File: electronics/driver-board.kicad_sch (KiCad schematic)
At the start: 61 parts, among them J1 Conn_01x18_Female, J3 Motor_Conn_01x04, J4 Screw_Terminals, J5 Conn_01x06_Female, SW1 RST_SW_Push, U1 ESP32-WROOM-E, U2 BA033CC0FP-E2, U4 AS5601-ASOT, U5 TMC2209-LA

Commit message: work on module prototype
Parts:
- removed C25: 10µF, Capacitor_SMD:C_0402_1005Metric, symbol Device:C_Small
- removed C30: 1µF, Capacitor_SMD:C_0402_1005Metric, symbol Device:C_Small
- removed C31, C32, C33: 100nF, Capacitor_SMD:C_0402_1005Metric, symbol Device:C_Small
- removed SW1: RST_SW_Push, Button_Switch_SMD:SW_SPST_B3U-1000P, symbol Switch:SW_Push
- removed TP10, TP11, TP12, TP13, TP14, TP15, TP6, TP7, TP8, TP9: TestPoint, TestPoint:TestPoint_Pad_D1.0mm, symbol Connector:TestPoint
- added J2: Conn_01x02_Socket, Connector_PinSocket_2.54mm:PinSocket_1x02_P2.54mm_Vertical, symbol Connector:Conn_01x02_Socket
- added J7, J8: Conn_01x08_Socket, Connector_PinSocket_2.54mm:PinSocket_1x08_P2.54mm_Vertical, symbol Connector:Conn_01x08_Socket
- added JP2: SolderJumper_3_Bridged12, Jumper:SolderJumper-3_P1.3mm_Bridged12_Pad1.0x1.5mm, symbol Jumper:SolderJumper_3_Bridged12
- added R2: 1K, Resistor_SMD:R_0805_2012Metric_Pad1.20x1.40mm_HandSolder, symbol Device:R_Small
- C10, C11, C12, C13, C14, C15, C16, C8, C9, TP3, TP4, U5: now not fitted; now left out of the parts list
- H2: now not fitted
- R1, R20, R21, R4: footprint Resistor_SMD:R_0402_1005Metric -> Resistor_SMD:R_0805_2012Metric_Pad1.20x1.40mm_HandSolder
- R11: value 1K -> 1K 1%; footprint Resistor_SMD:R_0201_0603Metric -> Resistor_SMD:R_0805_2012Metric_Pad1.20x1.40mm_HandSolder; now not fitted; now left out of the parts list
- R12, R13: footprint Resistor_SMD:R_2010_5025Metric -> Resistor_SMD:R_0805_2012Metric_Pad1.20x1.40mm_HandSolder; now not fitted; now left out of the parts list
- R19, R7: footprint Resistor_SMD:R_0402_1005Metric -> Resistor_SMD:R_0805_2012Metric_Pad1.20x1.40mm_HandSolder; now not fitted; now left out of the parts list
- R3: footprint Resistor_SMD:R_0603_1608Metric -> Resistor_SMD:R_0805_2012Metric_Pad1.20x1.40mm_HandSolder; now not fitted; now left out of the parts list
- R5: value 715K -> 1220K 1%; footprint Resistor_SMD:R_0402_1005Metric -> Resistor_SMD:R_0805_2012Metric_Pad1.20x1.40mm_HandSolder
- R6: value 110K -> 110K 1%; footprint Resistor_SMD:R_0402_1005Metric -> Resistor_SMD:R_0805_2012Metric_Pad1.20x1.40mm_HandSolder
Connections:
- net +3V3: now also R1.2, J8.7 (Pin_7); no longer R1.1
- net ESP_EN: now also R1.1; no longer R1.2
- net ESP_IO00: now also J2.1 (Pin_1)
- net ESP_IO02: now also J2.2 (Pin_2)
- net ESP_IO06: now also J7.1 (Pin_1)
- net ESP_IO12: now also JP2.2 (C), R2.2
- net ESP_IO13: now also R2.1
- net GND: now also J8.2 (Pin_2), J8.8 (Pin_8)
- net TMC2209_OA1: now also J8.4 (Pin_4)
- net TMC2209_OA2: now also J8.3 (Pin_3)
- net TMC2209_OB1: now also J8.5 (Pin_5)
- net TMC2209_OB2: now also J8.6 (Pin_6)
- net VBUS: now also J8.1 (Pin_1)
- new net TMC2209_CLK: J7.6 (Pin_6)
- new net TMC2209_DIR: J7.8 (Pin_8)
- new net TMC2209_MS1: J7.2 (Pin_2)
- new net TMC2209_MS2: J7.3 (Pin_3)
- new net TMC2209_PDN1: J7.4 (Pin_4), JP2.1 (A)
- new net TMC2209_PDN2: J7.5 (Pin_5), JP2.3 (B)
- new net TMC2209_STEP: J7.7 (Pin_7)
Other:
- note added: "EXPANSION HEADER"
- note added: "STEPPER DRIVER"
- note removed: "IO MAPPING AND EXPANSION HEADER"
- note removed: "STEPPER CONTROL"
- note removed: "from https://www.digikey.at/en/products/detail/trinamic-motion-control-gmbh/TMC2209-BOB/10490037"
- moved on the sheet: C1, C17, C2, C3, C4, C5, C6, C7, D1, D3, H1, H3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

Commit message: tmc5240/ad5074d/esp32c6 board to be ordered
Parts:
- removed C14: 100nF, Capacitor_SMD:C_0603_1608Metric, symbol Device:C_Polarized_Small
- removed C4: 1µF, Capacitor_SMD:C_0402_1005Metric, symbol Device:C_Small
- removed J1: Conn_01x18_Female, Connector_PinSocket_2.54mm:PinSocket_2x09_P2.54mm_Vertical, symbol Connector:Conn_01x18_Female
- removed J2: Conn_01x02_Socket, Connector_PinSocket_2.54mm:PinSocket_1x02_P2.54mm_Vertical, symbol Connector:Conn_01x02_Socket
- removed J4: Screw_Terminals, TerminalBlock_Phoenix:TerminalBlock_Phoenix_MKDS-1,5-2-5.08_1x02_P5.08mm_Horizontal, symbol Connector:Screw_Terminal_01x02
- removed J7, J8: Conn_01x08_Socket, Connector_PinSocket_2.54mm:PinSocket_1x08_P2.54mm_Vertical, symbol Connector:Conn_01x08_Socket
- removed JP2: SolderJumper_3_Bridged12, Jumper:SolderJumper-3_P1.3mm_Bridged12_Pad1.0x1.5mm, symbol Jumper:SolderJumper_3_Bridged12
- removed R12, R13: 100mR, Resistor_SMD:R_0805_2012Metric_Pad1.20x1.40mm_HandSolder, symbol Device:R_Small
- removed R19: 100K, Resistor_SMD:R_0805_2012Metric_Pad1.20x1.40mm_HandSolder, symbol Device:R_Small
- removed R20, R21: 4K7, Resistor_SMD:R_0805_2012Metric_Pad1.20x1.40mm_HandSolder, symbol Device:R_Small
- removed R5: 1220K 1%, Resistor_SMD:R_0805_2012Metric_Pad1.20x1.40mm_HandSolder, symbol Device:R_Small
- removed R6: 110K 1%, Resistor_SMD:R_0805_2012Metric_Pad1.20x1.40mm_HandSolder, symbol Device:R_Small
- removed U1: ESP32-WROOM-E, Espressif:ESP32-WROOM-32E, symbol Espressif:ESP32-WROOM-E
- removed U2: BA033CC0FP-E2, Package_TO_SOT_SMD:TO-252-2, symbol Slimc_Converter_DCDC:BAxxXX0
- removed U4: AS5601-ASOT, Package_SO:SOIC-8_3.9x4.9mm_P1.27mm, symbol Slimc_Sensor_Magnetic:AS5601-ASOT
- removed U5: TMC2209-LA, trinamic-footprints:QFN28P, symbol Slimc_Driver_Motor:TMC2209-LA
- added C14, C19, C31: 1µF, Capacitor_SMD:C_0603_1608Metric, symbol Device:C_Small
- added C18: 47µF, Capacitor_SMD:CP_Elec_5x5.9, symbol Device:C_Polarized_Small
- added C20, C26, C27: 22µF, Capacitor_SMD:C_0603_1608Metric, symbol Device:C_Small
- added C21: 4.7µF, Capacitor_SMD:C_0603_1608Metric, symbol Device:C_Small
- added C22: 22nF, Capacitor_SMD:C_0603_1608Metric, symbol Device:C_Small
- added C28, C29: 2.2µF, Capacitor_SMD:C_0603_1608Metric, symbol Device:C_Small
- added C30: 100nF, Capacitor_SMD:C_0603_1608Metric, symbol Device:C_Small
- added D2: DS210W, Diode_SMD:D_SOD-123F, symbol Device:D_Schottky_Small
- added D4: D_Small, symbol Device:D_Small
- added D6: DS210W, Diode_SMD:D_SOD-123F, symbol Device:D_Small
- added J1: Conn_01x02, Connector_TE-Connectivity:TE_2834006-2_1x02_P4.0mm_Horizontal, symbol Connector_Generic:Conn_01x02
- added L2: 10µH, Inductor_SMD:L_Vishay_IHLP-2020, symbol Device:L
- added R10: 17.4K, Resistor_SMD:R_0603_1608Metric, symbol Device:R_Small
- added R9: 100K, Resistor_SMD:R_0603_1608Metric, symbol Device:R_Small
- added SW1, SW2: SW_Push, Button_Switch_SMD:SW_SPST_B3U-1000P, symbol Switch:SW_Push
- added TP1, TP10, TP2, TP5, TP6, TP7, TP8, TP9: TestPoint, TestPoint:TestPoint_Pad_D1.0mm, symbol Connector:TestPoint
- added U2: LMR16020PDDAR, Package_SO:SOIC-8-1EP_3.9x4.9mm_P1.27mm_EP2.95x4.9mm_Mask2.71x3.4mm_ThermalVias, symbol Slimc_Converter_DCDC:LMR16020PDDAR
- added U3: ESP32-C6-MINI-1/U, Espressif:ESP32-C6-MINI-1, symbol Espressif:ESP32-C6-MINI-1/U
- added U4: AMS1117-3.3, Package_TO_SOT_SMD:SOT-223-3_TabPin2, symbol Regulator_Linear:AMS1117-3.3
- added U5: TMC5240-TSSOP38, Package_SO:HTSSOP-38-1EP_6.1x12.5mm_P0.65mm_EP5.2x12.5mm_Mask3.39x6.35mm_ThermalVias, symbol Slimc_Driver_Motor:TMC5240-TSSOP38
- added U6: MT6835, Package_SO:TSSOP-16_4.4x5mm_P0.65mm, symbol Slimc_Sensor_Magnetic:MT6835
- added U7: AS5047D, Package_SO:TSSOP-14_4.4x5mm_P0.65mm, symbol Sensor_Magnetic:AS5047D
- C1, C6: footprint Capacitor_SMD:C_0402_1005Metric -> Capacitor_SMD:C_0603_1608Metric
- C10: value 100nF -> 2.2µF; Voltage 50V -> 16V; now fitted; now in the parts list
- C11: value 22nF -> 100nF; footprint Capacitor_SMD:C_0805_2012Metric -> Capacitor_SMD:C_0603_1608Metric; now fitted; now in the parts list
- C12, C8, TP3, TP4: now fitted; now in the parts list
- C13: value 100nF -> 1µF; now fitted; now in the parts list
- C15: value 10µF -> 100nF; footprint Capacitor_SMD:C_1210_3225Metric -> Capacitor_SMD:C_0603_1608Metric; Voltage 50V -> (none)
- C16: value 10µF -> 4.7µF; footprint Capacitor_SMD:C_1210_3225Metric -> Capacitor_SMD:C_0603_1608Metric; Voltage 50V -> (none); now fitted; now in the parts list
- C3: value 10µF -> 100nF; footprint Capacitor_SMD:C_0402_1005Metric -> Capacitor_SMD:C_0603_1608Metric; Voltage 35V -> (none)
- C9: value 2.2µF -> 100nF; Voltage 6v3 -> 16V; now fitted; now in the parts list
- D1: footprint Slimc_LED_SMD:LED_WS2812C-2020 -> LED_SMD:LED_WS2812B-2020_PLCC4_2.0x2.0mm
- H2: now fitted
- J3: footprint Connector_JST:JST_EH_B4B-EH-A_1x04_P2.50mm_Vertical -> Connector_PinHeader_2.54mm:PinHeader_1x04_P2.54mm_Vertical
- J5: footprint Connector_PinSocket_2.54mm:PinSocket_2x03_P2.54mm_Vertical -> Connector_PinSocket_1.27mm:PinSocket_1x06_P1.27mm_Vertical
- R1: footprint Resistor_SMD:R_0805_2012Metric_Pad1.20x1.40mm_HandSolder -> Resistor_SMD:R_0603_1608Metric
- R11: value 1K 1% -> 4K7; footprint Resistor_SMD:R_0805_2012Metric_Pad1.20x1.40mm_HandSolder -> Resistor_SMD:R_0603_1608Metric; Tol 1% -> (none); now fitted; now in the parts list
- R2: value 1K -> 4K7; footprint Resistor_SMD:R_0805_2012Metric_Pad1.20x1.40mm_HandSolder -> Resistor_SMD:R_0603_1608Metric; Tol 1% -> (none)
- R3: value 0R100 -> 41.2K; footprint Resistor_SMD:R_0805_2012Metric_Pad1.20x1.40mm_HandSolder -> Resistor_SMD:R_0603_1608Metric; now fitted; now in the parts list
- R4: value 230R -> 10K; footprint Resistor_SMD:R_0805_2012Metric_Pad1.20x1.40mm_HandSolder -> Resistor_SMD:R_0603_1608Metric
- R7: value 20K -> 12K; footprint Resistor_SMD:R_0805_2012Metric_Pad1.20x1.40mm_HandSolder -> Resistor_SMD:R_0603_1608Metric; Tolerance (none) -> 1%; now fitted; now in the parts list
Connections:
- net ESP_IO06 is gone; now on net GND: R7.1
- net ESP_IO13 is gone; now on net +3V3: R11.1, R2.1
- net ESP_IO27 is gone; now on net +3V3: R4.1
- net +3V3: now also C15.2, C3.2, C9.2, R1.1, C21.2, C31.2, U3.3 (3V3), U4.2 (VO), U5.11 (VCC_IO), U6.9 (VDD), U7.11 (VDD), U7.12 (VDD3V3); no longer C1.1, C6.2, D1.1 (VDD), R1.2, R7.2
- net ESP_EN: now also C2.2, R4.2, SW1.2, U3.8 (EN/CHIP_PU); no longer C2.1, R1.1
- net GND: now also C10.1, C11.2, C15.1, C16.1, C2.1, C9.1, R3.1, C14.2, C18.2, C19.1, C20.1, C21.1, C26.1, C27.1, C28.1, C29.1, C30.1, C31.1, D2.2 (A), J1.1 (Pin_1), R10.1, SW1.1, SW2.1, U2.7 (GND), U2.9 (EP), U3.1 (GND), U3.11 (GND), U3.14 (GND), U3.2 (GND), U3.36 (GND), U3.37 (GND), U3.38 (GND), U3.39 (GND), U3.40 (GND), U3.41 (GND), U3.42 (GND), U3.43 (GND), U3.44 (GND), U3.45 (GND), U3.46 (GND), U3.47 (GND), U3.48 (GND), U3.49 (GND), U3.50 (GND), U3.51 (GND), U3.52 (GND), U3.53 (GND), U4.1 (GND), U5.10 (AGND), U5.27 (PGND1), U5.3 (CLK), U5.31 (PGND2), U5.39 (EP), U6.12 (GND), U7.13 (GND), U7.5 (TST); no longer C15.2, C16.2, C2.2, C6.1, C9.2, R3.2
- net VBUS: now also C11.1, C8.2, C14.1, C18.1, C28.2, C29.2, C30.2, J1.2 (Pin_2), U2.2 (VIN), U5.25 (VS1), U5.29 (VS2), U5.33 (VS3), U5.35 (SLEEP); no longer C10.1, C15.1, C16.1, C3.2, C8.1
- net at D1.4 (DIN): now also U3.5 (GPIO2/ADC1_CH2); no longer R4.2
- net at TP3.1: now also U3.27 (GPIO21)
- net at TP4.1: now also U3.28 (GPIO22)
- net at C10.2: now also U5.9 (VDD1V8)
- net ESP_IO00 renamed ESP_UART_TXD
- net ESP_UART_TXD: now also U3.31 (U0TXD/GPIO16)
- net ESP_IO01 renamed ESP_UART_RXD
- net ESP_UART_RXD: now also U3.30 (U0RXD/GPIO17)
- net ESP_IO03 renamed ESP_IO0
- net ESP_IO0: now also R1.2, SW2.2, U3.12 (GPIO0/ADC1_CH0/XTAL_32K_P)
- net ESP_IO12: no longer names the net of R2.2
- net ESP_IO12: now also U5.16 (UART_EN); no longer R11.2
- net TMC2209_OA1 renamed TMC_OUT2B
- net TMC_OUT2B: now also U5.28 (OUT2B)
- net TMC2209_OA2 renamed TMC_OUT1B
- net TMC_OUT1B: now also U5.26 (OUT1B)
- net TMC2209_OB1 renamed TMC_OUT2A
- net TMC_OUT2A: now also U5.30 (OUT2A)
- net TMC2209_OB2 renamed TMC_OUT1A
- net TMC_OUT1A: now also U5.32 (OUT1A)
- new net: C6.2, U2.1 (BOOT)
- new net: R3.2, U2.4 (RT/SYNC)
- new net: R10.2, R9.1, U2.5 (FB)
- new net: C6.1, D2.1 (K), L2.1, U2.8 (SW)
- new net: TP9.1, U3.23 (GPIO9)
- new net: TP10.1, U3.24 (GPIO18)
- new net: TP5.1, U3.29 (GPIO23)
- new net: U5.13 (ENCB), U7.6 (B)
- new net: U5.14 (ENCA), U7.7 (A)
- new net: TP1.1, U3.25 (GPIO19)
- new net: TP6.1, U3.6 (GPIO3/ADC1_CH3)
- new net: C22.1, U5.22 (CPO)
- new net: C22.2, U5.20 (CPI)
- new net: R7.2, U5.7 (IREF)
- new net: C8.1, U5.23 (VCP)
- new net: TP2.1, U3.26 (GPIO20)
- new net: TP8.1, U3.15 (MTCK/GPIO6/ADC1_CH6)
- new net: TP7.1, U3.16 (MTDO/GPIO7)
- new net +5V: C1.1, C16.2, C19.2, C20.2, C26.2, C27.2, D1.1 (VDD), L2.2, R9.2, U4.3 (VI)
- new net ENC_A / TMC_ENCA: U6.16 (A)
- new net ENC_B / TMC_ENCB: U6.15 (B)
- new net ENC_Z: U6.14 (Z)
- new net SPI_CSN_ENC: U3.22 (GPIO8), U6.8 (CS), U7.1 (~{CS})
- new net SPI_CSN_TMC: U3.20 (GPIO15), U5.36 (CS/AD2)
- new net SPI_SCK: U3.19 (GPIO14), U5.38 (SCK/AD1), U6.7 (SCK), U7.2 (CLK)
- new net SPI_SDI: U3.18 (GPIO13/USB_D+), U5.1 (SDI/AD0), U6.6 (MOSI), U7.4 (MOSI)
- new net SPI_SDO: U3.17 (GPIO12/USB_D-), U5.2 (SDO/NAO), U6.5 (MISO), U7.3 (MISO)
- new net TMC_DIAG0: U3.10 (MTDI/GPIO5/ADC1_CH5), U5.17 (DIAG0)
- new net TMC_DIAG1: U3.9 (MTMS/GPIO4/ADC1_CH4), U5.18 (DIAG1/SW)
- new net TMC_ENABLE: R11.2, U3.13 (GPIO1/ADC1_CH1/XTAL_32K_N), U5.15 (DRV_EN)
- new net TMC_ENCN: U5.12 (ENCN)
- no-connect marks 13 -> 18
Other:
- note added: "1A"
- note added: "2A"
- note added: "600kHz"
- note added: "POWER"
- note added: "Remove to enable SPI"
- note removed: "(RSA,RSB) = 2010 1W"
- note removed: "Delay boot ~50µs"
- note removed: "EXPANSION HEADER"
- note removed: "INTERRUPTS"
- note removed: "MAIN CONTROL UNIT"
- note removed: "MAX 25V"
- note removed: "MAX 5A LOAD"
- note removed: "MOUNTING"
- note removed: "POWER CONNECTORS"
- note removed: "POWER SUPPLY"
- note removed: "STATUS LED"
- note removed: "STEPPER DRIVER"
- note removed: "STEPPER FEEDBACK"
- note removed: "Source sensing"
- moved on the sheet: C1, C17, C2, C5, C7, D1, D3, H1, H3, H4, J3, J5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

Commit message: changed some 0402 caps to 0603
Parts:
- C17, C2, C5, C7: footprint Capacitor_SMD:C_0402_1005Metric -> Capacitor_SMD:C_0603_1608Metric
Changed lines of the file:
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@@
       (effects (font (size 1.27 1.27)))
     )
-    (property "Footprint" "Capacitor_SMD:C_0402_1005Metric" (at 313.69 49.53 0)
+    (property "Footprint" "Capacitor_SMD:C_0603_1608Metric" (at 313.69 49.53 0)
       (effects (font (size 1.27 1.27)) hide)
     )
@@
       (effects (font (size 1.27 1.27)))
     )
-    (property "Footprint" "Capacitor_SMD:C_0402_1005Metric" (at 265.43 64.77 0)
+    (property "Footprint" "Capacitor_SMD:C_0603_1608Metric" (at 265.43 64.77 0)
       (effects (font (size 1.27 1.27)) hide)
     )
@@
       (effects (font (size 1.27 1.27)))
     )
-    (property "Footprint" "Capacitor_SMD:C_0402_1005Metric" (at 318.77 49.53 0)
+    (property "Footprint" "Capacitor_SMD:C_0603_1608Metric" (at 318.77 49.53 0)
       (effects (font (size 1.27 1.27)) hide)
     )
@@
       (effects (font (size 1.27 1.27)))
     )
-    (property "Footprint" "Capacitor_SMD:C_0402_1005Metric" (at 308.61 49.53 0)
-      (effects (font (size 1.27 1.27)) hide)
-    )
+    (property "Footprint" "Capacitor_SMD:C_0603_1608Metric" (at 308.61 49.53 0)
+      (effects (font (size 1.27 1.27)) hide)
+    )

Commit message: changed motor connector to jst-xh
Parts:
- J3: footprint Connector_PinHeader_2.54mm:PinHeader_1x04_P2.54mm_Vertical -> Connector_JST:JST_XH_S4B-XH-A-1_1x04_P2.50mm_Horizontal; digikey_part_number 455-1613-ND -> 455-2243-ND; mfr_part_number B4B-EH-A(LF)(SN) -> S4B-XH-A
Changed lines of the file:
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@@
       (effects (font (size 1.27 1.27)) (justify left))
     )
-    (property "Footprint" "Connector_PinHeader_2.54mm:PinHeader_1x04_P2.54mm_Vertical" (at 154.94 134.62 0)
+    (property "Footprint" "Connector_JST:JST_XH_S4B-XH-A-1_1x04_P2.50mm_Horizontal" (at 154.94 134.62 0)
       (effects (font (size 1.27 1.27)) hide)
     )
@@
       (effects (font (size 1.27 1.27)) hide)
     )
-    (property "mfr_part_number" "B4B-EH-A(LF)(SN)" (at 154.94 134.62 0)
+    (property "mfr_part_number" "S4B-XH-A" (at 154.94 134.62 0)
       (effects (font (size 1.27 1.27)) hide)
     )
-    (property "digikey_part_number" "455-1613-ND" (at 154.94 134.62 0)
+    (property "digikey_part_number" "455-2243-ND" (at 154.94 134.62 0)
       (effects (font (size 1.27 1.27)) hide)
     )

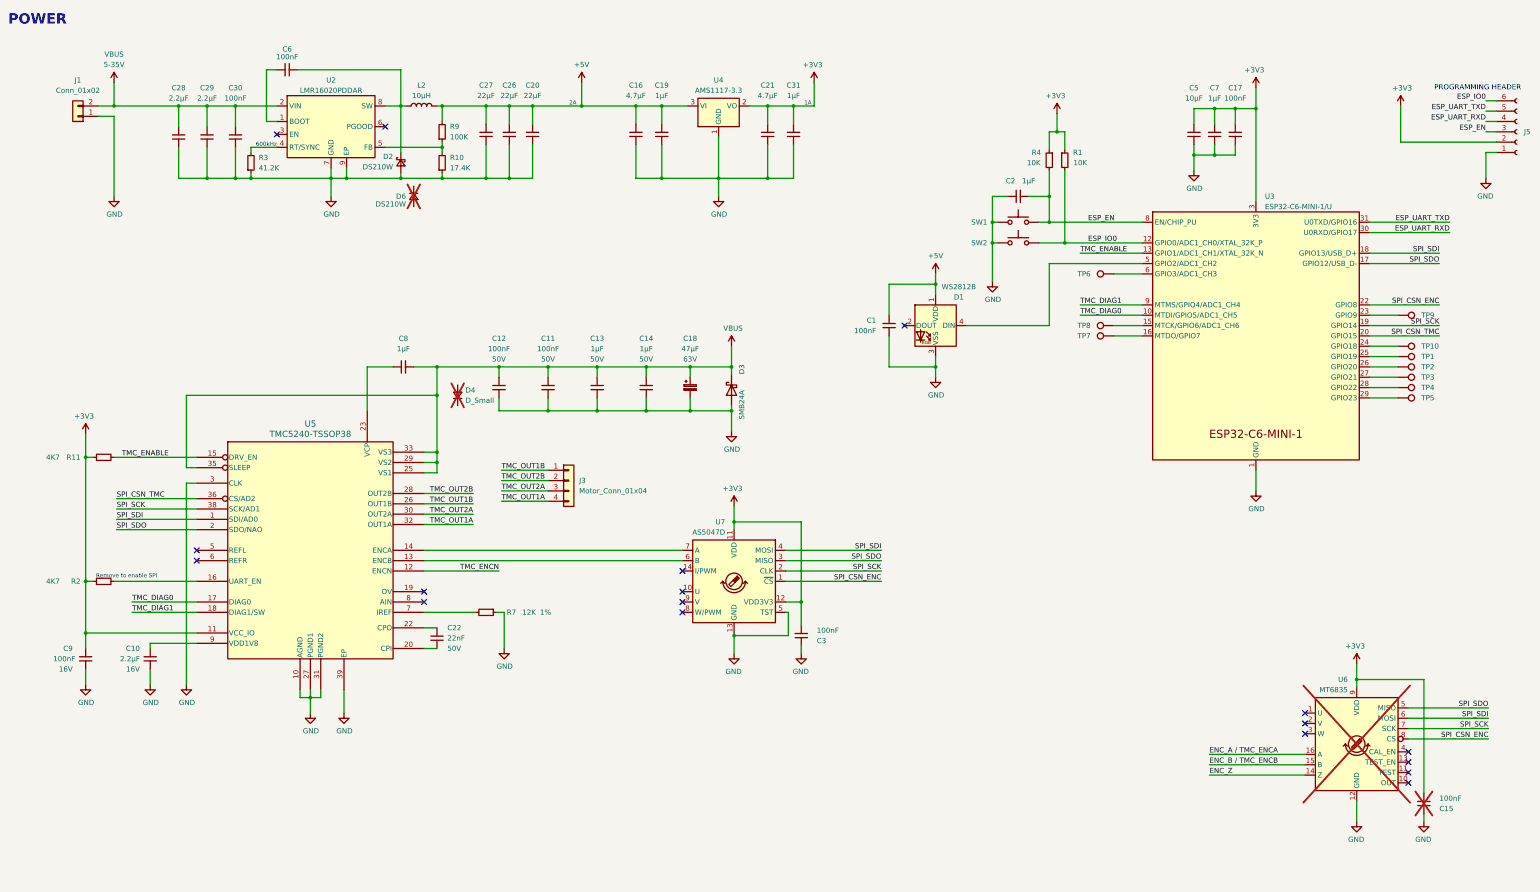
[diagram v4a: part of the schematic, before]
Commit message: filled in part numbers
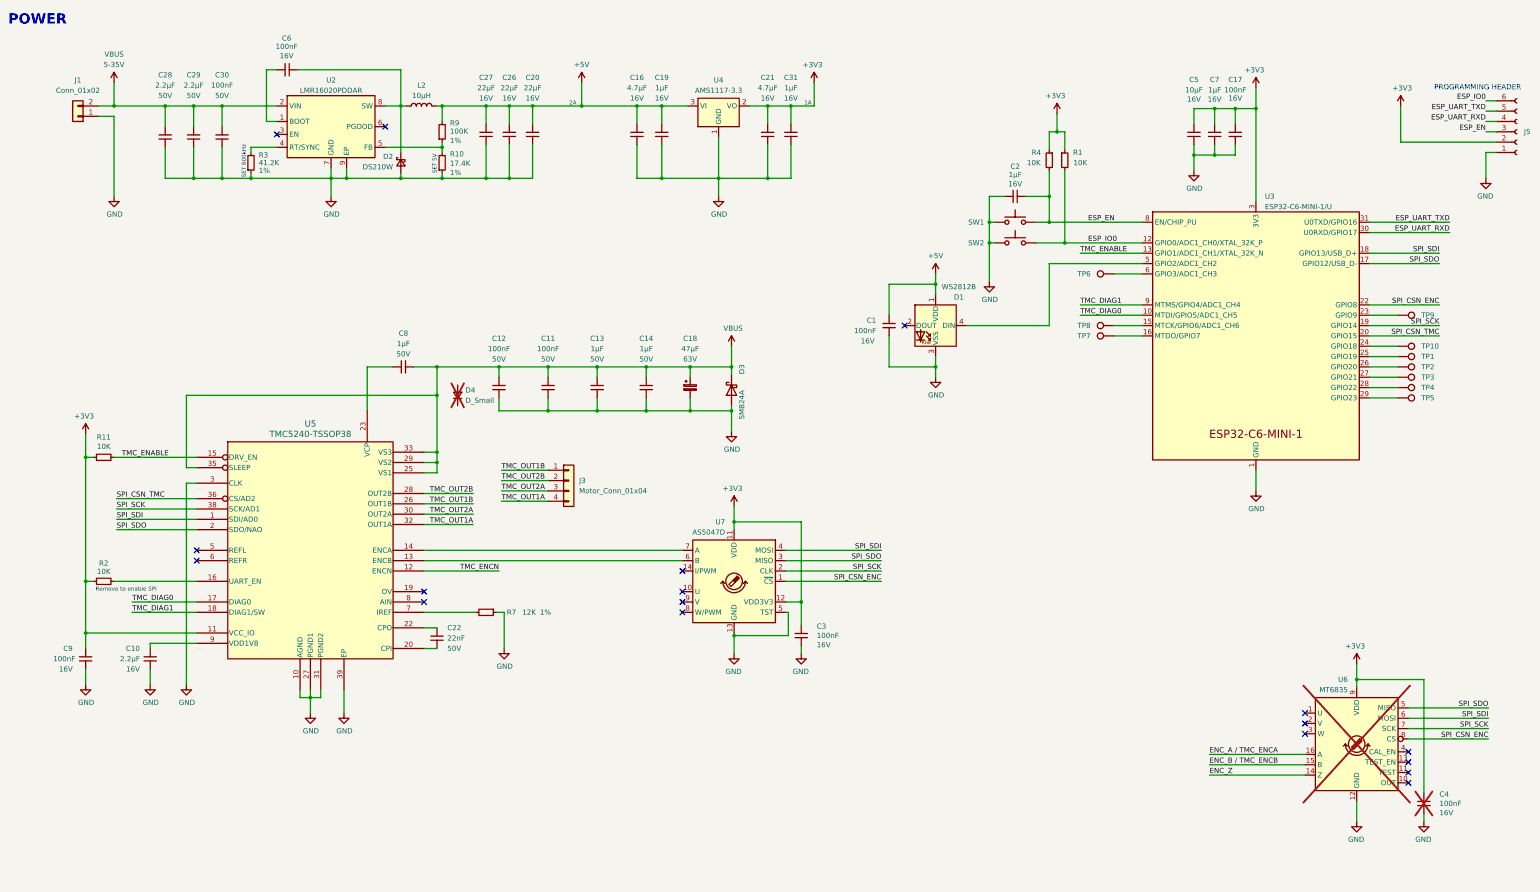
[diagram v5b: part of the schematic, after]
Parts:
- removed C15: 100nF, Capacitor_SMD:C_0603_1608Metric, symbol Device:C_Small
- removed D6: DS210W, Diode_SMD:D_SOD-123F, symbol Device:D_Small
- added C4: 100nF, Capacitor_SMD:C_0603_1608Metric, symbol Device:C_Small
- C1, C17, C3, C6: Voltage (none) -> 16V; lcsc_part_number (none) -> C66501; mfr_part_number (none) -> CL10B104KO8NNNC
- C10: lcsc_part_number (none) -> C23630; mfr_part_number (none) -> CL10A225KO8NNNC
- C11, C12: lcsc_part_number (none) -> C1591; mfr_part_number (none) -> CL10B104KB8NNNC
- C13, C14, C8: lcsc_part_number (none) -> C15849; mfr_part_number (none) -> CL10A105KB8NNNC
- C16, C21: Voltage (none) -> 16V; lcsc_part_number (none) -> C19666; mfr_part_number (none) -> CL10A475KO8NNNC
- C19, C2, C31, C7: Voltage (none) -> 16V; lcsc_part_number (none) -> C1592; mfr_part_number (none) -> CL10A105KO8NNNC
- C20, C26, C27: Voltage (none) -> 16V; lcsc_part_number (none) -> C2762594; mfr_part_number (none) -> CL10A226MO7JZNC
- C22: lcsc_part_number (none) -> C21122; mfr_part_number (none) -> CL10B223KB8NNNC
- C28, C29: Voltage (none) -> 50V; lcsc_part_number (none) -> C913904; mfr_part_number (none) -> CL10A225KB8NNNC
- C30: Voltage (none) -> 50V; lcsc_part_number (none) -> C1591; mfr_part_number (none) -> CL10B104KB8NNNC
- C5: Voltage (none) -> 16V; lcsc_part_number (none) -> C92487; mfr_part_number (none) -> CL10A106MO8NQNC
- C9: lcsc_part_number (none) -> C66501; mfr_part_number (none) -> CL10B104KO8NNNC
- D2: lcsc_part_number (none) -> C116100; mfr_part_number (none) -> DS210W
- J1: lcsc_part_number (none) -> C86483; mfr_part_number (none) -> 2834006-2
- J3: lcsc_part_number (none) -> C157925
- L2: lcsc_part_number (none) -> C844996; mfr_part_number (none) -> IHLP2020CZER100M01
- R1, R4: lcsc_part_number (none) -> C4226066; mfr_part_number (none) -> RT0603FRE1310KL
- R10: Tolerance (none) -> 1%; lcsc_part_number (none) -> C863611; mfr_part_number (none) -> RT0603FRE0717K4L
- R11, R2: value 4K7 -> 10K; lcsc_part_number (none) -> C4226066; mfr_part_number (none) -> RT0603FRE1310KL
- R3: Tolerance (none) -> 1%; lcsc_part_number (none) -> C706173; mfr_part_number (none) -> RT0603FRE0741K2L
- R7: lcsc_part_number (none) -> C136933; mfr_part_number (none) -> RT0603FRE0712KL
- R9: Tolerance (none) -> 1%; lcsc_part_number (none) -> C728638; mfr_part_number (none) -> RT0603FRE07100KL
- SW1, SW2: lcsc_part_number (none) -> C231329; mfr_part_number (none) -> B3U-1000P
- U2: lcsc_part_number (none) -> C190006; mfr_part_number (none) -> LMR16020PDDAR
- U3: lcsc_part_number (none) -> C5736265; mfr_part_number (none) -> ESP32-C6-MINI-1-N4
- U4: lcsc_part_number (none) -> C5181460; mfr_part_number (none) -> AMS1117-3.3
- U5: mfr_part_number (none) -> TMC5240AUU+
- U6: lcsc_part_number (none) -> C2932578; mfr_part_number (none) -> MT6835GT-STD
- U7: lcsc_part_number (none) -> C962063; mfr_part_number (none) -> AS5047P-ATSM
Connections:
- net +3V3: now also C4.2
- net GND: now also C4.1
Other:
- note added: "SET 5V"
- note added: "SET 600kHz"
- note removed: "600kHz"
- moved on the sheet: C2, C28, C29, C30, C31, SW1, SW2
